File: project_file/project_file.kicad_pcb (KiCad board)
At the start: 2 copper layers, 44 x 84 mm, 76 parts, among them IC1 BMI055, J1 Power Module 1, J10 CAP & ADC IN, J11 SPI Port, J12 I2C A, J13 FMU PWM OUT, J14 PPM RC, J15 2908-05WB-MG, J16 RC, J17 SBUS, J18 IO/PWM out, J2 Power Module 2, J3 USB, J4 Telemetry 1, J5 Telemetry 2, J6 UART & I2C B, J7 CAN 1, J8 CAN 2, J9 GPS Module, U1 STM32F765IIKx, U10 TJA1051TK-3, U11 LT3080xDD, U12 LP5907MFX-3.3, U13 LP5907MFX-3.3, U3 IST8310, U4 ICM-20602, U5 ICM-20689, U6 MS5611-01BA, U8 STM32F103V8Tx, U9 TJA1051TK-3, Y1 ABM2-8.000MHZ-D4Y-T

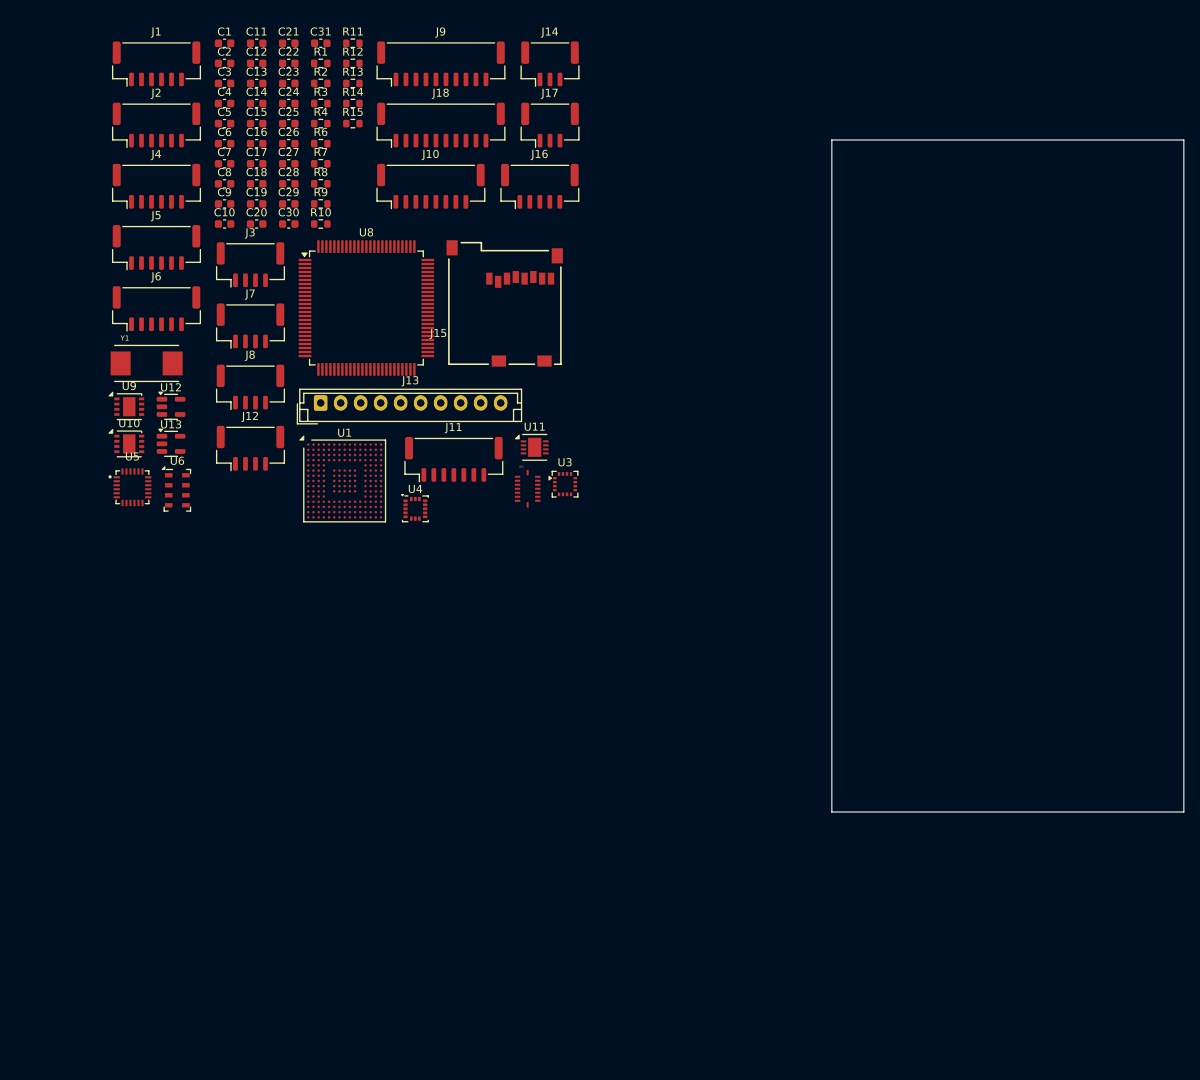
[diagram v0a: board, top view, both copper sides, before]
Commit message: Grouped U19 (can transceiver 1) components together
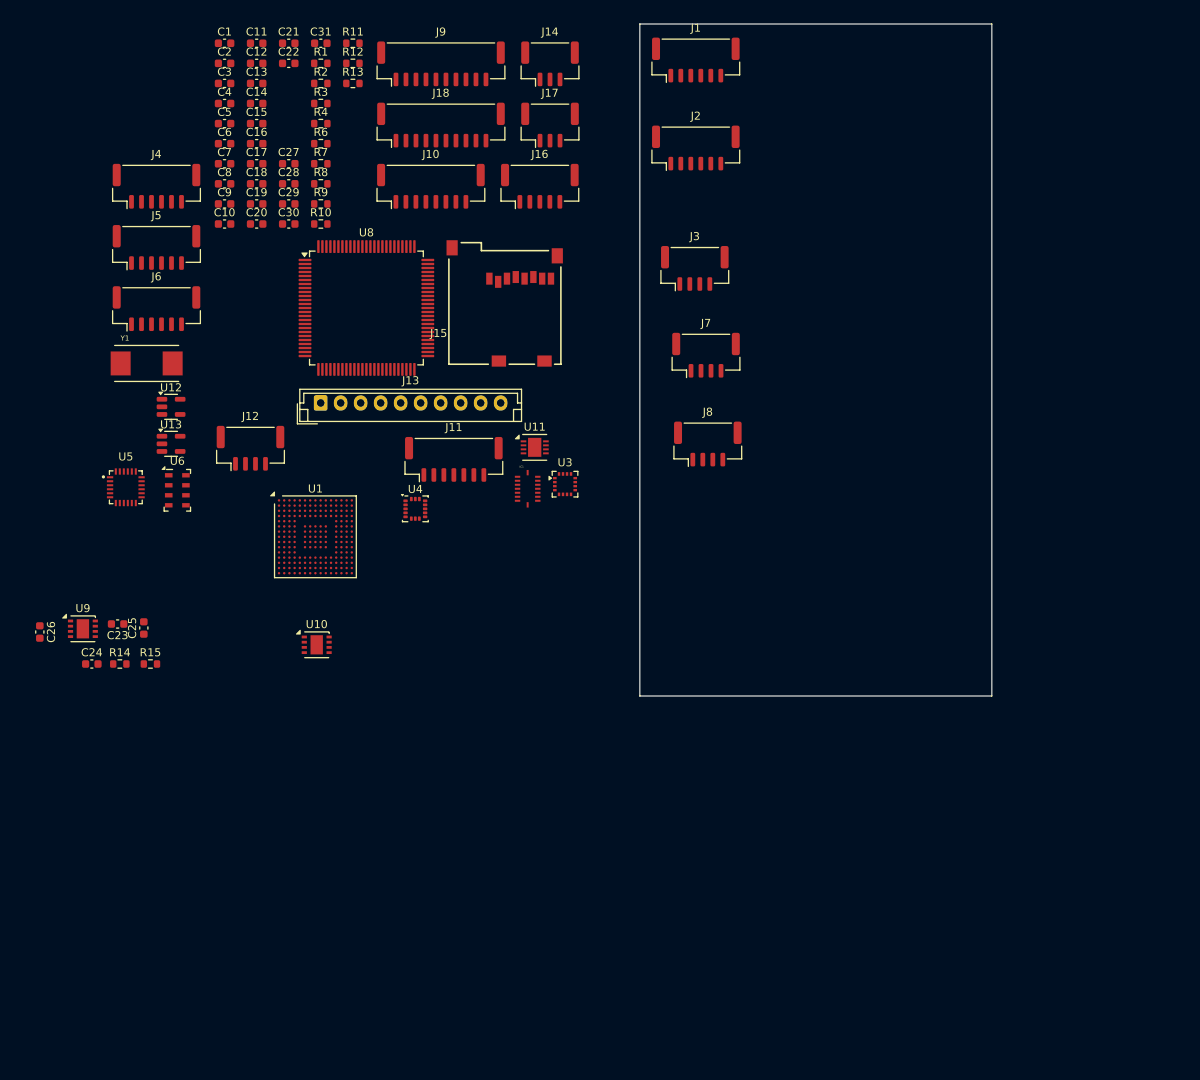
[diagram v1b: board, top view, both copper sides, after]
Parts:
- moved R14 75.9 mm to (42.0, 110.0)
- moved C24 74.3 mm to (38.5, 110.0)
- moved R15 72.1 mm to (45.8, 110.0)
- moved C23 70.9 mm to (41.7, 105.0), turned to 180 degrees
- moved C26 68.5 mm to (32.0, 106.0), turned to -90 degrees
- moved J2 67.5 mm to (114.0, 45.5)
- moved J1 67.4 mm to (114.0, 34.5)
- moved C25 65.6 mm to (45.0, 105.5), turned to 90 degrees
- moved J8 57.6 mm to (115.5, 82.5)
- moved J7 57.1 mm to (115.3, 71.4)
- moved J3 55.5 mm to (113.9, 60.5)
- moved U10 34.3 mm to (66.6, 107.6)
- moved U9 28.4 mm to (37.4, 105.6)
- moved U1 7.88 mm to (66.5, 94.1)
- moved U5 0.83 mm to (42.8, 87.9)

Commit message: more grouping
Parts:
- moved C21 95.2 mm to (43.3, 125.5), turned to 180 degrees
- moved C5 92.4 mm to (92.0, 127.2), turned to -90 degrees
- moved C6 90.6 mm to (95.2, 126.2)
- moved R13 89.0 mm to (43.5, 122.0)
- moved C8 88.7 mm to (95.3, 129.0)
- moved R12 87.6 mm to (46.5, 119.0), turned to -90 degrees
- moved C14 86.9 mm to (72.4, 125.8), turned to 180 degrees
- moved C7 86.7 mm to (89.2, 127.2), turned to -90 degrees
- moved C22 86.0 mm to (43.0, 118.5)
- moved C15 83.7 mm to (67.2, 125.8), turned to 180 degrees
- moved C27 78.7 mm to (34.5, 120.8), turned to -90 degrees
- moved C20 70.4 mm to (46.5, 124.3), turned to -90 degrees
- moved U5 59.6 mm to (91.8, 121.7)
- moved Y1 54.7 mm to (69.5, 121.5)
- moved U10 30.9 mm to (38.6, 120.6)
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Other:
- board text added: "CAN1"
- board text added: "CAN2"
- board text added: "ICM-20689"
- board text added: "OSCILLATOR"

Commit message: more grouping
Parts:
- moved R11 128.7 mm to (43.8, 158.2), turned to -90 degrees
- moved R7 114.7 mm to (36.4, 158.0), turned to -90 degrees
- moved R8 111.4 mm to (40.0, 158.0), turned to -90 degrees
- moved R9 111.4 mm to (32.2, 158.2), turned to -90 degrees
- moved C31 107.0 mm to (64.9, 139.4), turned to 90 degrees
- moved R10 104.9 mm to (48.4, 158.2), turned to -90 degrees
- moved J15 95.0 mm to (39.0, 145.0)
- moved C1 91.1 mm to (85.6, 118.3), turned to -90 degrees
- moved C3 85.6 mm to (80.8, 119.1)
- moved C30 82.2 mm to (61.5, 137.2)
- moved C2 78.2 mm to (81.0, 108.7), turned to 180 degrees
- moved C4 75.7 mm to (81.0, 111.1), turned to 180 degrees
- moved C29 75.0 mm to (58.1, 127.3), turned to 180 degrees
- moved C28 74.2 mm to (57.5, 123.9), turned to -90 degrees
- moved U13 60.6 mm to (61.1, 141.8)
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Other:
- board text added: "3V3 REG"
- board text added: "5V REG"
- board text added: "ICM-20602"
- board text added: "MICRO SD"

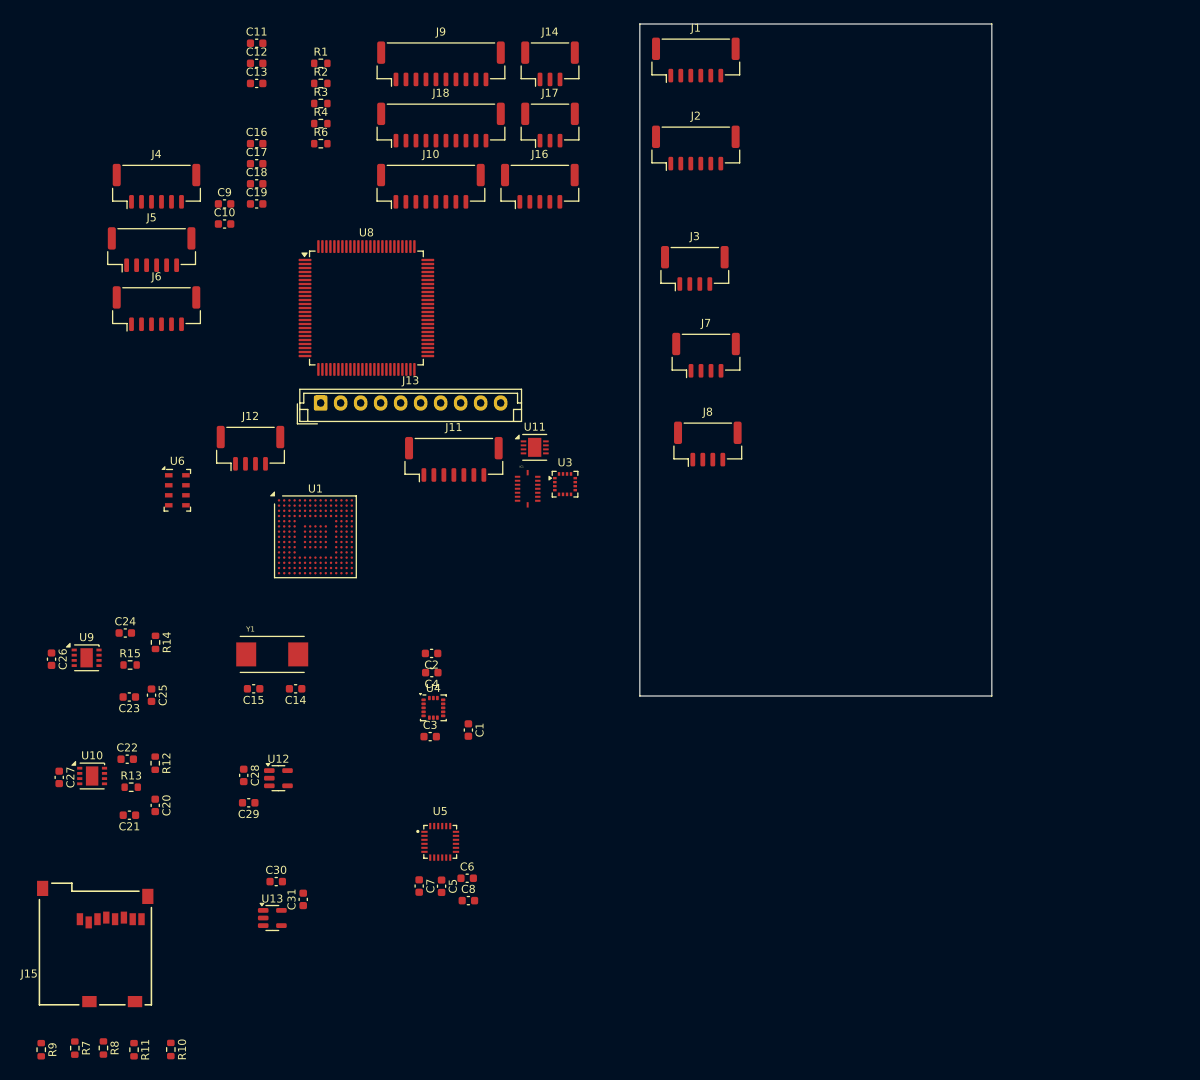
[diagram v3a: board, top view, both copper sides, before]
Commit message: Ports added
ive added the ports and a few ic's on the back
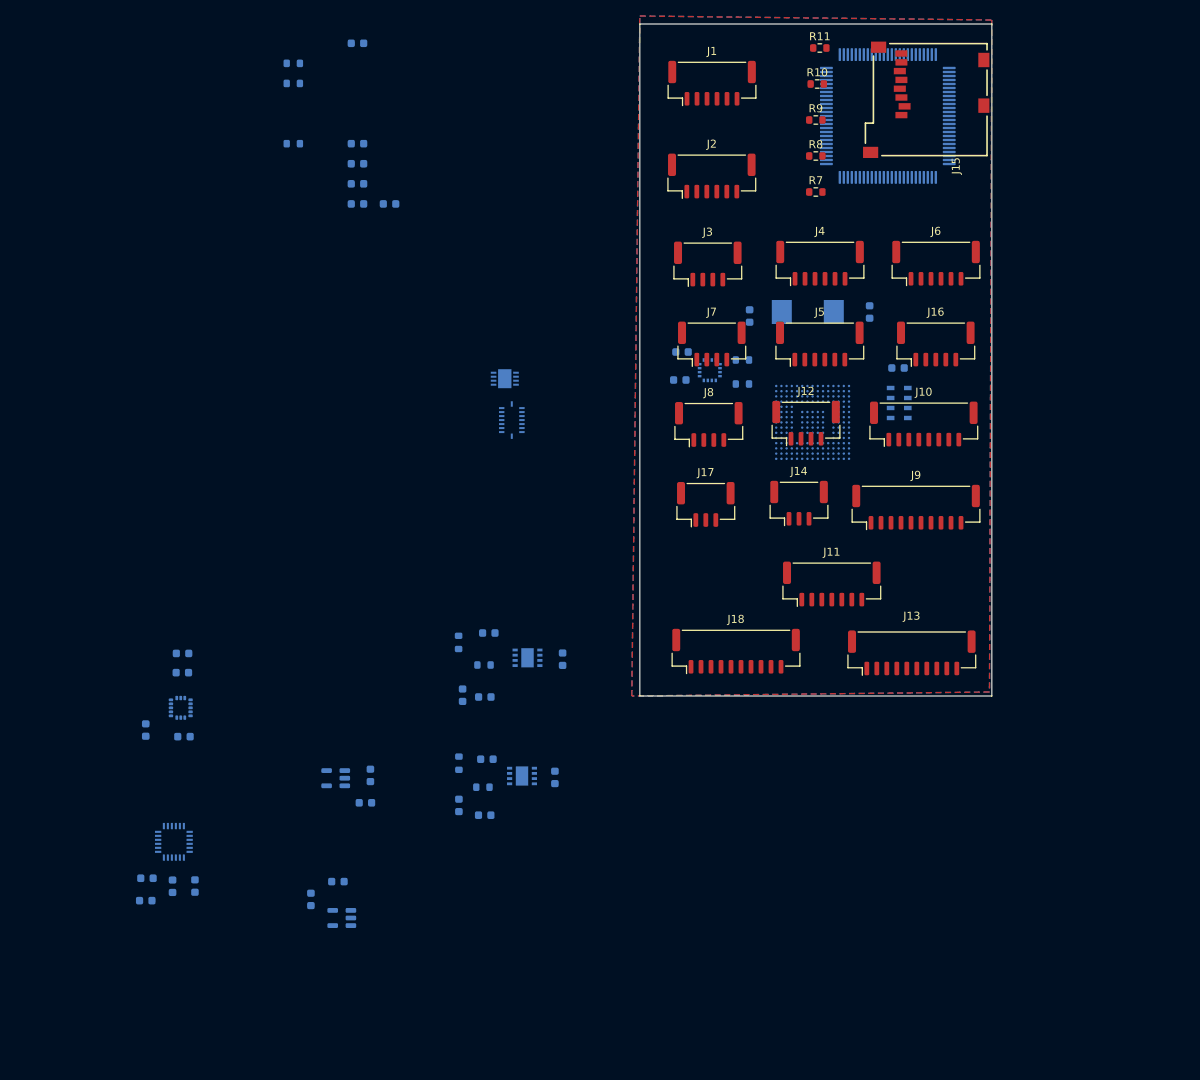
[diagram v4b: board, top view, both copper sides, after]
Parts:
- C1, C10, C11, C12, C13, C14, C15, C16, C17, C18, C19, C2, C20, C21, C22, C23, C24, C25, C26, C27, C28, C29, C3, C30, C31, C4, C5, C6, C7, C8, C9, IC1, R1, R12, R13, R14, R15, R2, R3, R4, R6, U1, U10, U11, U12, U13, U3, U4, U5, U6, U8, U9, Y1: moved to B.Cu
- moved R11 151.7 mm to (129.5, 33.0), turned to 0 degrees
- moved R9 151.3 mm to (129.0, 42.0), turned to 0 degrees
- moved J15 148.1 mm to (142.8, 39.5), turned to 90 degrees
- moved R10 145.2 mm to (129.2, 37.5), turned to 0 degrees
- moved R8 142.7 mm to (129.0, 46.5), turned to 0 degrees
- moved R7 141.5 mm to (129.0, 51.0), turned to 0 degrees
- moved J6 97.6 mm to (144.0, 59.9)
- moved U6 90.9 mm to (139.4, 77.4), turned to 180 degrees
- moved C10 86.1 mm to (139.3, 73.0), turned to 180 degrees
- moved C14 85.8 mm to (135.7, 66.0), turned to -90 degrees
- moved J5 84.4 mm to (129.5, 70.0)
- moved J4 83.5 mm to (129.5, 59.9)
- moved J9 81.2 mm to (141.5, 90.4)
- moved J13 80.0 mm to (141.0, 108.0)
- moved Y1 79.5 mm to (128.0, 66.0)
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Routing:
- added copper zone on B.Cu, net GND
- added copper zone on F.Cu, net GND
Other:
- board text added: "FMU PWM OUT"
- board text added: "J13"

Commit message: -
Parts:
- moved C25 56.2 mm to (94.3, 58.5), turned to 180 degrees
- moved C24 44.2 mm to (130.7, 94.5)
- moved C26 40.9 mm to (133.5, 90.3)
- moved U9 39.9 mm to (127.9, 89.9), turned to 0 degrees
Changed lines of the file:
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@@
 			(psa4output no)
 			(plot_black_and_white yes)
+			(plotinvisibletext no)
 			(sketchpadsonfab no)
 			(plotpadnumbers no)
@@
 	(footprint "Capacitor_SMD:C_0603_1608Metric"
 		(layer "B.Cu")
-		(at 88.1235 106.125 180)
+		(at 130.725 94.5 180)
 		(descr "Capacitor SMD 0603 (1608 Metric), square (rectangular) end terminal, IPC_7351 nominal, (Body size source: IPC-SM-782 page 76, https://www.pcb-3d.com/wordpress/wp-content/uploads/ipc-sm-782a_amendment_1_and_2.pdf), generated with kicad-footprint-generator")
 		(tags "capacitor")
@@
 	(footprint "Capacitor_SMD:C_0603_1608Metric"
 		(layer "B.Cu")
-		(at 84.8485 113.9 -90)
+		(at 94.275 58.5 180)
 		(descr "Capacitor SMD 0603 (1608 Metric), square (rectangular) end terminal, IPC_7351 nominal, (Body size source: IPC-SM-782 page 76, https://www.pcb-3d.com/wordpress/wp-content/uploads/ipc-sm-782a_amendment_1_and_2.pdf), generated with kicad-footprint-generator")
 		(tags "capacitor")
 		(property "Reference" "C25"
-			(at 0 1.43 90)
+			(at 0 1.43 0)
 			(layer "B.SilkS")
 			(effects
@@
 		)
 		(property "Value" "4.7nF"
-			(at 0 -1.43 90)
+			(at 0 -1.43 0)
 			(layer "B.Fab")
 			(effects
@@
 		)
 		(property "Datasheet" ""
-			(at 0 0 90)
+			(at 0 0 0)
 			(unlocked yes)
 			(layer "B.Fab")
@@
 		)
 		(property "Description" "Unpolarized capacitor, small symbol"
-			(at 0 0 90)
+			(at 0 0 0)
 			(unlocked yes)
 			(layer "B.Fab")
@@
 		)
 		(fp_line
-			(start -1.48 0.73)
-			(end 1.48 0.73)
+			(start 1.48 0.73)
+			(end 1.48 -0.73)
 			(stroke
 				(width 0.05)
@@
 		)
 		(fp_line
-			(start 1.48 0.73)
-			(end 1.48 -0.73)
+			(start 1.48 -0.73)
+			(end -1.48 -0.73)
 			(stroke
 				(width 0.05)
@@
 		)
 		(fp_line
-			(start -1.48 -0.73)
-			(end -1.48 0.73)
+			(start -1.48 0.73)
+			(end 1.48 0.73)
 			(stroke
 				(width 0.05)
@@
 		)
 		(fp_line
-			(start 1.48 -0.73)
-			(end -1.48 -0.73)
+			(start -1.48 -0.73)
+			(end -1.48 0.73)
 			(stroke
 				(width 0.05)
@@
 		)
 		(fp_line
-			(start -0.8 0.4)
-			(end 0.8 0.4)
+			(start 0.8 0.4)
+			(end 0.8 -0.4)
 			(stroke
 				(width 0.1)
@@
 		)
 		(fp_line
-			(start 0.8 0.4)
-			(end 0.8 -0.4)
+			(start 0.8 -0.4)
+			(end -0.8 -0.4)
 			(stroke
 				(width 0.1)
@@
 		)
 		(fp_line
-			(start -0.8 -0.4)
-			(end -0.8 0.4)
+			(start -0.8 0.4)
+			(end 0.8 0.4)
 			(stroke
 				(width 0.1)
@@
 		)
 		(fp_line
-			(start 0.8 -0.4)
-			(end -0.8 -0.4)
+			(start -0.8 -0.4)
+			(end -0.8 0.4)
 			(stroke
 				(width 0.1)
@@
 		)
 		(fp_text user "${REFERENCE}"
-			(at 0 0 90)
+			(at 0 0 0)
 			(layer "B.Fab")
 			(effects
@@
 		)
 		(pad "1" smd roundrect
-			(at -0.775 0 270)
+			(at -0.775 0 180)
 			(size 0.9 0.95)
 			(layers "B.Cu" "B.Mask" "B.Paste")
@@
 		)
 		(pad "2" smd roundrect
-			(at 0.775 0 270)
+			(at 0.775 0 180)
 			(size 0.9 0.95)
 			(layers "B.Cu" "B.Mask" "B.Paste")
@@
 	(footprint "Capacitor_SMD:C_0603_1608Metric"
 		(layer "B.Cu")
-		(at 97.3485 109.4 -90)
+		(at 133.5 90.275 -90)
 		(descr "Capacitor SMD 0603 (1608 Metric), square (rectangular) end terminal, IPC_7351 nominal, (Body size source: IPC-SM-782 page 76, https://www.pcb-3d.com/wordpress/wp-content/uploads/ipc-sm-782a_amendment_1_and_2.pdf), generated with kicad-footprint-generator")
 		(tags "capacitor")
@@
 	(footprint "Package_DFN_QFN:DFN-8-1EP_3x3mm_P0.65mm_EP1.55x2.4mm"
 		(layer "B.Cu")
-		(at 92.961 109.225 180)
+		(at 127.8875 89.9)
 		(descr "8-Lead Plastic Dual Flat, No Lead Package (MF) - 3x3x0.9 mm Body [DFN] (see Microchip Packaging Specification 00000049BS.pdf)")
 		(tags "DFN 0.65")
@@
 		)
 		(property "Datasheet" "http://www.nxp.com/docs/en/data-sheet/TJA1051.pdf"
-			(at 0 0 0)
+			(at 0 0 180)
 			(unlocked yes)
 			(layer "B.Fab")
@@
 		)
 		(property "Description" "High-Speed CAN Transceiver, separate VIO, silent mode, DFN-8"
-			(at 0 0 0)
+			(at 0 0 180)
 			(unlocked yes)
 			(layer "B.Fab")
@@
 		(attr smd)
 		(fp_line
-			(start 1.56 1.56)
-			(end 1.56 1.41)
+			(start -1.5 -1.61)
+			(end 1.5 -1.61)
 			(stroke
 				(width 0.12)
@@
 		)
 		(fp_line
-			(start -1.5 -1.61)
-			(end 1.5 -1.61)
+			(start 1.56 1.56)
+			(end 1.56 1.41)
 			(stroke
 				(width 0.12)
@@
 		)
 		(fp_line
-			(start 2.13 1.4)
-			(end 2.13 -1.4)
+			(start -2.13 1.4)
+			(end -2.13 -1.4)
 			(stroke
 				(width 0.05)
@@
 		)
 		(fp_line
-			(start 1.75 1.75)
-			(end 1.75 1.4)
+			(start -1.75 -1.75)
+			(end -1.75 -1.4)
 			(stroke
 				(width 0.05)
@@
 		)
 		(fp_line
-			(start 1.75 1.4)
-			(end 2.13 1.4)
+			(start -1.75 -1.75)
+			(end 1.75 -1.75)
 			(stroke
 				(width 0.05)
@@
 		)
 		(fp_line
-			(start 1.75 -1.4)
-			(end 2.13 -1.4)
+			(start -1.75 -1.4)
+			(end -2.13 -1.4)
 			(stroke
 				(width 0.05)
@@
 		)
 		(fp_line
-			(start 1.75 -1.75)
-			(end 1.75 -1.4)
+			(start -1.75 1.4)
+			(end -2.13 1.4)
 			(stroke
 				(width 0.05)
@@
 		(fp_line
 			(start -1.75 1.75)
-			(end 1.75 1.75)
+			(end -1.75 1.4)
 			(stroke
 				(width 0.05)
@@
 		(fp_line
 			(start -1.75 1.75)
-			(end -1.75 1.4)
+			(end 1.75 1.75)
 			(stroke
 				(width 0.05)
@@
 		)
 		(fp_line
-			(start -1.75 1.4)
-			(end -2.13 1.4)
+			(start 1.75 -1.75)
+			(end 1.75 -1.4)
 			(stroke
 				(width 0.05)
@@
 		)
 		(fp_line
-			(start -1.75 -1.4)
-			(end -2.13 -1.4)
+			(start 1.75 -1.4)
+			(end 2.13 -1.4)
 			(stroke
 				(width 0.05)
@@
 		)
 		(fp_line
-			(start -1.75 -1.75)
-			(end 1.75 -1.75)
+			(start 1.75 1.4)
+			(end 2.13 1.4)
 			(stroke
 				(width 0.05)
@@
 		)
 		(fp_line
-			(start -1.75 -1.75)
-			(end -1.75 -1.4)
+			(start 1.75 1.75)
+			(end 1.75 1.4)
 			(stroke
 				(width 0.05)
@@
 		)
 		(fp_line
-			(start -2.13 1.4)
-			(end -2.13 -1.4)
+			(start 2.13 1.4)
+			(end 2.13 -1.4)
 			(stroke
 				(width 0.05)
@@
 		)
 		(fp_line
-			(start 1.5 1.5)
-			(end 1.5 -1.5)
+			(start -1.5 -1.5)
+			(end -1.5 0.75)
 			(stroke
 				(width 0.1)
@@
 		)
 		(fp_line
-			(start 1.5 -1.5)
-			(end -1.5 -1.5)
+			(start -1.5 0.75)
+			(end -0.75 1.5)
 			(stroke
 				(width 0.1)
@@
 		)
 		(fp_line
-			(start -1.5 0.75)
-			(end -0.75 1.5)
+			(start 1.5 -1.5)
+			(end -1.5 -1.5)
 			(stroke
 				(width 0.1)
@@
 		)
 		(fp_line
-			(start -1.5 -1.5)
-			(end -1.5 0.75)
+			(start 1.5 1.5)
+			(end 1.5 -1.5)
 			(stroke
 				(width 0.1)
@@
 		)
 		(pad "" smd rect
-			(at -0.3875 -0.6 180)
+			(at -0.3875 -0.6)
 			(size 0.6 1)
 			(layers "B.Paste")
 		)
 		(pad "" smd rect
-			(at -0.3875 0.6 180)
+			(at -0.3875 0.6)
 			(size 0.6 1)
 			(layers "B.Paste")
 		)
 		(pad "" smd rect
-			(at 0.3875 -0.6 180)
+			(at 0.3875 -0.6)
 			(size 0.6 1)
 			(layers "B.Paste")
 		)
 		(pad "" smd rect
-			(at 0.3875 0.6 180)
+			(at 0.3875 0.6)
 			(size 0.6 1)
 			(layers "B.Paste")
 		)
 		(pad "1" smd rect
-			(at -1.55 0.975 180)
+			(at -1.55 0.975)
 			(size 0.65 0.35)
 			(layers "B.Cu" "B.Mask" "B.Paste")
@@
 		)
 		(pad "2" smd rect
-			(at -1.55 0.325 180)
+			(at -1.55 0.325)
 			(size 0.65 0.35)
 			(layers "B.Cu" "B.Mask" "B.Paste")
@@
 		)
 		(pad "3" smd rect
-			(at -1.55 -0.325 180)
+			(at -1.55 -0.325)
 			(size 0.65 0.35)
 			(layers "B.Cu" "B.Mask" "B.Paste")
@@
 		)
 		(pad "4" smd rect
-			(at -1.55 -0.975 180)
+			(at -1.55 -0.975)
 			(size 0.65 0.35)
 			(layers "B.Cu" "B.Mask" "B.Paste")
@@
 		)
 		(pad "5" smd rect
-			(at 1.55 -0.975 180)
+			(at 1.55 -0.975)
 			(size 0.65 0.35)
 			(layers "B.Cu" "B.Mask" "B.Paste")
@@
 		)
 		(pad "6" smd rect
-			(at 1.55 -0.325 180)
+			(at 1.55 -0.325)
 			(size 0.65 0.35)
 			(layers "B.Cu" "B.Mask" "B.Paste")
@@
 		)
 		(pad "7" smd rect
-			(at 1.55 0.325 180)
+			(at 1.55 0.325)
 			(size 0.65 0.35)
 			(layers "B.Cu" "B.Mask" "B.Paste")
@@
 		)
 		(pad "8" smd rect
-			(at 1.55 0.975 180)
+			(at 1.55 0.975)
 			(size 0.65 0.35)
 			(layers "B.Cu" "B.Mask" "B.Paste")
@@
 		)
 		(pad "9" smd rect
-			(at 0 0 180)
+			(at 0 0)
 			(size 1.55 2.4)
 			(layers "B.Cu" "B.Mask")
